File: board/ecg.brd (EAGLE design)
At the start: 52.5 x 35.4 mm, 44 parts, among them IC1 SC189C, J1 USB_MICRO, J2 PROG, J3 JTAG, J4 2_PIN_JST-XH, J5 UART, J6 GND, J7 SPI, U1 ADAS1000, U2 CC3200MOD, X1 FH12-32S-0.5SH, Y1 8.192MHz

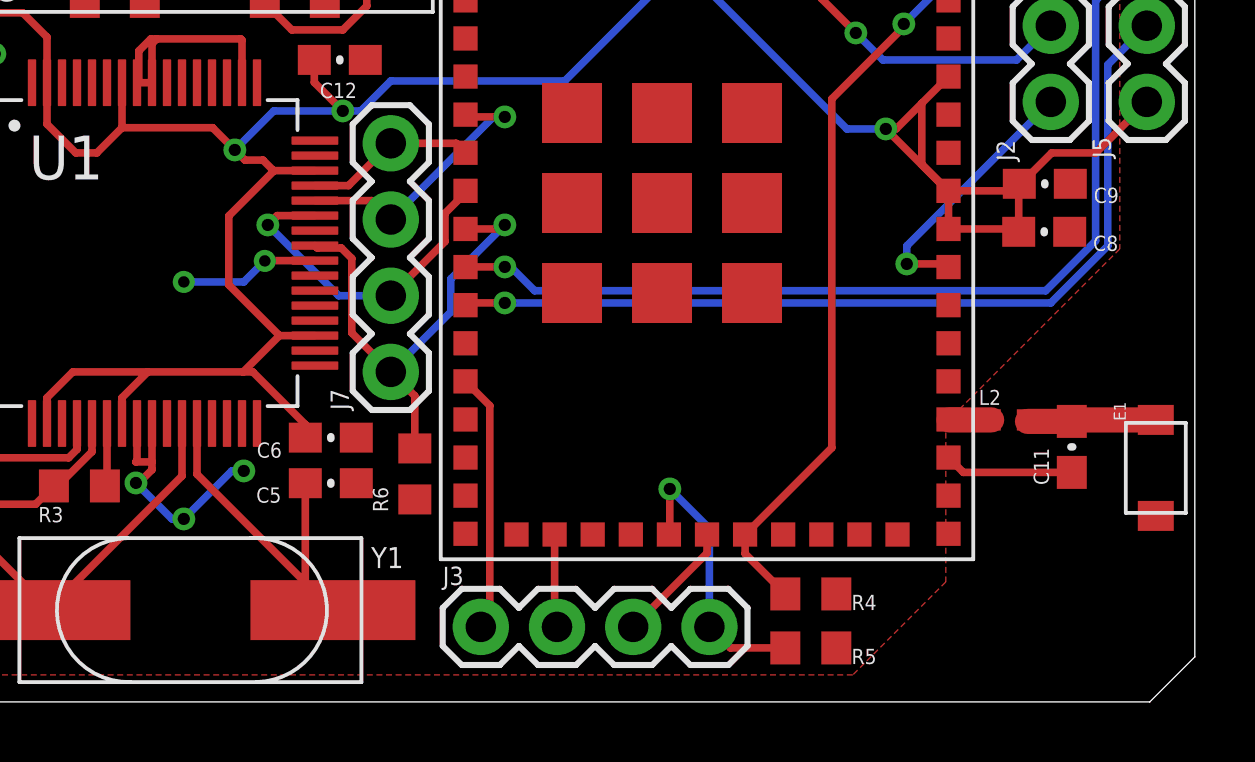
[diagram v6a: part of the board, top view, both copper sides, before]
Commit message: make sure pullup for !CS
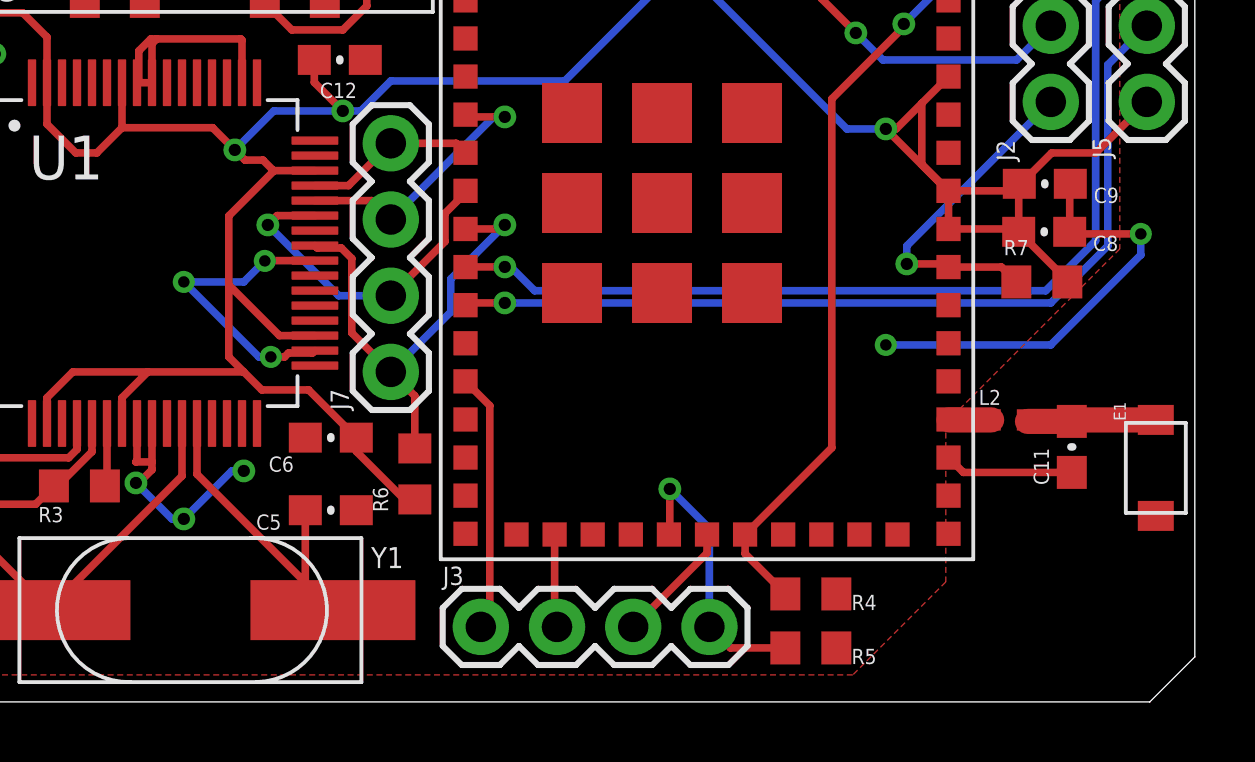
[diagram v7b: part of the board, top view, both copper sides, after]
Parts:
- added R7: (no value), scono:R0603
- moved C5 0.90 mm to (23.7, 6.39)
- turned C6 to 0 degrees
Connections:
- net 3.3V: now also R6.1, R7.2
- net GND: no longer R6.1
- net NRESET: now also R7.1
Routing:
- net GND: track 47.5 -> 67.5 mm, vias 7 -> 10
- net 3.3V: track 111.7 -> 119.9 mm
- net NRESET: track 8.82 -> 11.3 mm
- net N$7: track 12.7 -> 11.8 mm
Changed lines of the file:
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@@
 <attribute name="VALUE" x="11.33" y="6.407" size="0.508" layer="27" font="vector" rot="R180"/>
 </element>
-<element name="C5" library="scono" package="0603-CAP" value="18pF" x="23.7" y="7.29" smashed="yes">
-<attribute name="NAME" x="22.05" y="7.148" size="0.508" layer="25" font="vector" ratio="10" rot="R180"/>
-<attribute name="PIE-INT-REF-NUM" value="CAPACITOR-GENERIC" x="23.7" y="7.29" size="1.778" layer="27" display="off"/>
-<attribute name="VALUE" x="22.43" y="5.893" size="0.508" layer="27" font="vector"/>
-</element>
-<element name="C6" library="scono" package="0603-CAP" value="10uF" x="23.7" y="8.81" smashed="yes" rot="R180">
-<attribute name="NAME" x="22.07" y="8.648" size="0.508" layer="25" font="vector" ratio="10" rot="R180"/>
-<attribute name="PIE-INT-REF-NUM" value="CAPACITOR-GENERIC" x="23.7" y="8.81" size="1.778" layer="27" rot="R180" display="off"/>
-<attribute name="VALUE" x="24.97" y="10.207" size="0.508" layer="27" font="vector" rot="R180"/>
+<element name="C5" library="scono" package="0603-CAP" value="18pF" x="23.7" y="6.39" smashed="yes">
+<attribute name="NAME" x="22.05" y="6.248" size="0.508" layer="25" font="vector" ratio="10" rot="R180"/>
+<attribute name="PIE-INT-REF-NUM" value="CAPACITOR-GENERIC" x="23.7" y="6.39" size="1.778" layer="27" display="off"/>
+<attribute name="VALUE" x="22.43" y="4.993" size="0.508" layer="27" font="vector"/>
+</element>
+<element name="C6" library="scono" package="0603-CAP" value="10uF" x="23.7" y="8.81" smashed="yes">
+<attribute name="NAME" x="21.63" y="7.672" size="0.508" layer="25" font="vector" ratio="10"/>
+<attribute name="PIE-INT-REF-NUM" value="CAPACITOR-GENERIC" x="23.7" y="8.81" size="1.778" layer="27" display="off"/>
+<attribute name="VALUE" x="22.43" y="7.413" size="0.508" layer="27" font="vector"/>
 </element>
 <element name="C7" library="scono" package="0603-CAP" value="10uF" x="9.6" y="22.97" smashed="yes">
@@
 <attribute name="PACKAGE" value="R0603" x="26.5" y="7.6" size="1.778" layer="27" rot="R90" display="off"/>
 <attribute name="VALUE" x="27.516" y="6.33" size="0.508" layer="27" font="vector" rot="R90" align="top-left"/>
+</element>
+<element name="R7" library="scono" package="R0603" value="" x="47.4" y="14" smashed="yes">
+<attribute name="DESCRIPTION" value="RESISTOR, American symbol" x="47.4" y="14" size="1.778" layer="27" display="off"/>
+<attribute name="DISTRIBUTOR" value="DigiKey" x="47.4" y="14" size="1.778" layer="27" display="off"/>
+<attribute name="DISTRIBUTOR_PART_NUMBER" value="" x="47.4" y="14" size="1.778" layer="27" display="off"/>
+<attribute name="MANUFACTURER" value="Rohm Semiconductor" x="47.4" y="14" size="1.778" layer="27" display="off"/>
+<attribute name="MANUFACTURER_PART_NUMBER" value="" x="47.4" y="14" size="1.778" layer="27" display="off"/>
+<attribute name="NAME" x="46.13" y="14.889" size="0.508" layer="25" font="vector" ratio="10"/>
+<attribute name="NOTES" value="Cut Tape" x="47.4" y="14" size="1.778" layer="27" display="off"/>
+<attribute name="PACKAGE" value="R0603" x="47.4" y="14" size="1.778" layer="27" display="off"/>
+<attribute name="VALUE" x="46.13" y="12.984" size="0.508" layer="27" font="vector" align="top-left"/>
 </element>
 </elements>
@@
 <wire x1="48.4" y1="7.65" x2="44.785" y2="7.65" width="0.254" layer="1"/>
 <wire x1="44.785" y1="7.65" x2="44.29" y2="8.145" width="0.254" layer="1"/>
-<contactref element="R6" pad="1"/>
 <wire x1="23.17" y1="14.71" x2="21.51" y2="14.71" width="0.254" layer="1"/>
 <wire x1="21.51" y1="14.71" x2="21.5" y2="14.7" width="0.254" layer="1"/>
@@
 <wire x1="20.8" y1="14" x2="18.8" y2="14" width="0.254" layer="16"/>
 <via x="18.8" y="14" extent="1-16" drill="0.381"/>
+<via x="21.7" y="11.5" extent="1-16" drill="0.381"/>
+<wire x1="23.17" y1="11.71" x2="23.0894" y2="11.6294" width="0.254" layer="1"/>
+<wire x1="23.0894" y1="11.6294" x2="22.2882125" y2="11.6294" width="0.254" layer="1"/>
+<wire x1="22.2882125" y1="11.6294" x2="22.1588125" y2="11.5" width="0.254" layer="1"/>
+<wire x1="22.1588125" y1="11.5" x2="21.7" y2="11.5" width="0.254" layer="1"/>
+<wire x1="21.7" y1="11.5" x2="21.3" y2="11.5" width="0.254" layer="16"/>
+<wire x1="21.3" y1="11.5" x2="18.8" y2="14" width="0.254" layer="16"/>
+<wire x1="48.33" y1="15.67" x2="48.4" y2="15.6" width="0.254" layer="1"/>
+<wire x1="48.4" y1="15.6" x2="50.7" y2="15.6" width="0.254" layer="1"/>
+<via x="50.7" y="15.6" extent="1-16" drill="0.381"/>
+<wire x1="50.7" y1="15.6" x2="50.7" y2="14.9" width="0.254" layer="16"/>
+<wire x1="47.7" y1="11.9" x2="42.2" y2="11.9" width="0.254" layer="16"/>
+<via x="42.2" y="11.9" extent="1-16" drill="0.381"/>
+<wire x1="50.7" y1="14.9" x2="47.7" y2="11.9" width="0.254" layer="16"/>
+<wire x1="48.35" y1="17.27" x2="48.33" y2="17.25" width="0.254" layer="1"/>
+<wire x1="48.33" y1="17.25" x2="48.33" y2="15.67" width="0.254" layer="1"/>
 </signal>
 <signal name="N$4">
@@
 <wire x1="19.24" y1="7.59" x2="23.77" y2="3.06" width="0.254" layer="1"/>
 <wire x1="23.77" y1="3.06" x2="22.85" y2="3.98" width="0.254" layer="1"/>
-<wire x1="22.85" y1="3.98" x2="22.85" y2="7.29" width="0.254" layer="1"/>
+<wire x1="22.85" y1="3.98" x2="22.85" y2="6.39" width="0.254" layer="1"/>
 </signal>
 <signal name="3.3V">
@@
 <wire x1="21.81" y1="17.71" x2="23.17" y2="17.71" width="0.254" layer="1"/>
 <wire x1="21.99" y1="12.21" x2="23.17" y2="12.21" width="0.254" layer="1"/>
-<wire x1="21.99" y1="12.21" x2="20.78" y2="11" width="0.254" layer="1"/>
+<wire x1="20.79" y1="11.01" x2="20.78" y2="11" width="0.254" layer="1"/>
 <wire x1="20.78" y1="11" x2="17.6" y2="11" width="0.254" layer="1"/>
 <wire x1="17.6" y1="11" x2="16.74" y2="10.14" width="0.254" layer="1"/>
@@
 <wire x1="15.1" y1="11" x2="17.6" y2="11" width="0.254" layer="1"/>
 <wire x1="14.24" y1="10.14" x2="15.1" y2="11" width="0.254" layer="1"/>
-<wire x1="20.78" y1="11" x2="21.1" y2="11" width="0.254" layer="1"/>
 <wire x1="44.29" y1="15.765" x2="44.5" y2="15.765" width="0.254" layer="1"/>
 <wire x1="44.5" y1="15.765" x2="46.535" y2="15.765" width="0.254" layer="1"/>
@@
 <wire x1="21.8" y1="17.7" x2="20.3" y2="16.2" width="0.254" layer="1"/>
 <wire x1="20.3" y1="16.2" x2="20.3" y2="13.9" width="0.254" layer="1"/>
-<wire x1="21.1" y1="11" x2="22.85" y2="9.25" width="0.254" layer="1"/>
-<wire x1="22.85" y1="9.25" x2="22.85" y2="8.81" width="0.254" layer="1"/>
 <wire x1="23.15" y1="20.65" x2="23.15" y2="21.4" width="0.254" layer="1"/>
+<contactref element="R6" pad="1"/>
+<wire x1="24.55" y1="8.81" x2="22.96" y2="10.4" width="0.254" layer="1"/>
+<wire x1="21.4" y1="10.4" x2="20.79" y2="11.01" width="0.254" layer="1"/>
+<wire x1="22.96" y1="10.4" x2="21.4" y2="10.4" width="0.254" layer="1"/>
+<wire x1="24.55" y1="8.81" x2="24.55" y2="8.35" width="0.254" layer="1"/>
+<wire x1="26.15" y1="6.75" x2="26.5" y2="6.75" width="0.254" layer="1"/>
+<wire x1="24.55" y1="8.35" x2="26.15" y2="6.75" width="0.254" layer="1"/>
+<wire x1="20.3" y1="13.9" x2="20.3" y2="11.5" width="0.254" layer="1"/>
+<wire x1="20.3" y1="11.5" x2="20.79" y2="11.01" width="0.254" layer="1"/>
+<contactref element="R7" pad="2"/>
+<wire x1="46.63" y1="15.67" x2="48.25" y2="14.05" width="0.254" layer="1"/>
+<wire x1="48.25" y1="14.05" x2="48.25" y2="14" width="0.254" layer="1"/>
 </signal>
 <signal name="ADAS_CS">
@@
 <wire x1="42.9" y1="14.6" x2="44.185" y2="14.6" width="0.254" layer="1"/>
 <wire x1="44.185" y1="14.6" x2="44.29" y2="14.495" width="0.254" layer="1"/>
+<contactref element="R7" pad="1"/>
+<wire x1="46.55" y1="14" x2="46.055" y2="14.495" width="0.254" layer="1"/>
+<wire x1="46.055" y1="14.495" x2="44.29" y2="14.495" width="0.254" layer="1"/>
 </signal>
 <signal name="SOP2">
